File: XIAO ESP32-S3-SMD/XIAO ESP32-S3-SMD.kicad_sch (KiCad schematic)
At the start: 12 parts, among them J1 Conn_01x04_Socket, J2 Conn_01x03_Socket, J3 Conn_01x04_Socket, J4 Conn_01x03_Socket, J5 Conn_01x03_Socket, J6 Conn_01x02_Pin, U2 XIAO-ESP32-S3-SMD

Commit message: ライブラリ用ディレクトリの作成
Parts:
- J1, J3: footprint Connector_JST:JST_XH_B4B-XH-AM_1x04_P2.50mm_Vertical -> Connector_JST:JST_XH_B4B-XH-A_1x04_P2.50mm_Vertical
- J2, J4, J5: footprint Connector_JST:JST_XH_B3B-XH-AM_1x03_P2.50mm_Vertical -> Connector_JST:JST_XH_B3B-XH-A_1x03_P2.50mm_Vertical
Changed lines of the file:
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@@
 			)
 		)
-		(property "Footprint" "Connector_JST:JST_XH_B3B-XH-AM_1x03_P2.50mm_Vertical"
+		(property "Footprint" "Connector_JST:JST_XH_B3B-XH-A_1x03_P2.50mm_Vertical"
 			(at 284.48 34.29 0)
 			(hide yes)
@@
 			)
 		)
-		(property "Footprint" "Connector_JST:JST_XH_B4B-XH-AM_1x04_P2.50mm_Vertical"
+		(property "Footprint" "Connector_JST:JST_XH_B4B-XH-A_1x04_P2.50mm_Vertical"
 			(at 294.64 130.81 0)
 			(hide yes)
@@
 			)
 		)
-		(property "Footprint" "Connector_JST:JST_XH_B3B-XH-AM_1x03_P2.50mm_Vertical"
+		(property "Footprint" "Connector_JST:JST_XH_B3B-XH-A_1x03_P2.50mm_Vertical"
 			(at 284.48 66.04 0)
 			(hide yes)
@@
 			)
 		)
-		(property "Footprint" "Connector_JST:JST_XH_B4B-XH-AM_1x04_P2.50mm_Vertical"
+		(property "Footprint" "Connector_JST:JST_XH_B4B-XH-A_1x04_P2.50mm_Vertical"
 			(at 294.64 118.11 0)
 			(hide yes)
@@
 			)
 		)
-		(property "Footprint" "Connector_JST:JST_XH_B3B-XH-AM_1x03_P2.50mm_Vertical"
+		(property "Footprint" "Connector_JST:JST_XH_B3B-XH-A_1x03_P2.50mm_Vertical"
 			(at 284.48 50.8 0)
 			(hide yes)

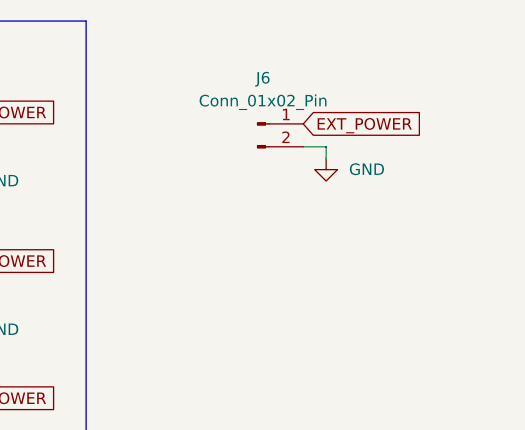
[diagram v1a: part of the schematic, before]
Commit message: 電源ライン配線前
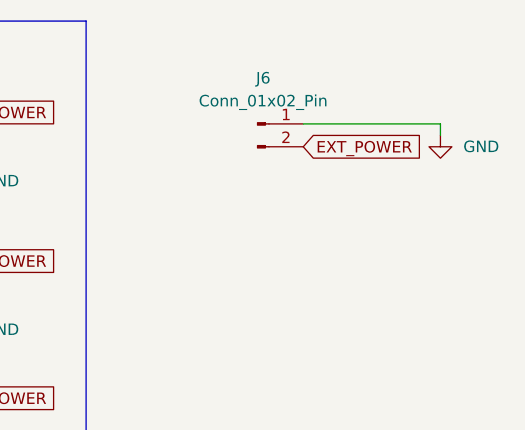
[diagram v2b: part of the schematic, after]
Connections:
- net EXT_POWER: now also J6.2 (Pin_2); no longer J6.1 (Pin_1)
- net GND: now also J6.1 (Pin_1); no longer J6.2 (Pin_2)
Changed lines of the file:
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@@
-	(wire
-		(pts
-			(xy 330.2 35.56) (xy 332.74 35.56)
-		)
-		(stroke
-			(width 0)
-			(type default)
-		)
-	)
 	(wire
 		(pts
@@
 	(wire
 		(pts
+			(xy 345.44 33.02) (xy 330.2 33.02)
+		)
+		(stroke
+			(width 0)
+			(type default)
+		)
+	)
+	(wire
+		(pts
 			(xy 203.2 107.95) (xy 196.85 107.95)
 		)
@@
 	(wire
 		(pts
-			(xy 332.74 35.56) (xy 332.74 36.83)
+			(xy 345.44 33.02) (xy 345.44 34.29)
 		)
 		(stroke
@@
 		)
 	)
+	(global_label "EXT_POWER"
+		(shape input)
+		(at 330.2 35.56 0)
+		(fields_autoplaced yes)
+		(effects
+			(font
+				(size 1.27 1.27)
+			)
+			(justify left)
+		)
+		(property "Intersheetrefs" "${INTERSHEET_REFS}"
+			(at 343.9498 35.56 0)
+			(hide yes)
+			(show_name no)
+			(do_not_autoplace no)
+			(effects
+				(font
+					(size 1.27 1.27)
+				)
+				(justify left)
+			)
+		)
+	)
 	(global_label "GPIO5"
 		(shape input)
@@
 		(property "Intersheetrefs" "${INTERSHEET_REFS}"
 			(at 223.6628 54.61 0)
-			(hide yes)
-			(show_name no)
-			(do_not_autoplace no)
-			(effects
-				(font
-					(size 1.27 1.27)
-				)
-				(justify left)
-			)
-		)
-	)
-	(global_label "EXT_POWER"
-		(shape input)
-		(at 330.2 33.02 0)
-		(fields_autoplaced yes)
-		(effects
-			(font
-				(size 1.27 1.27)
-			)
-			(justify left)
-		)
-		(property "Intersheetrefs" "${INTERSHEET_REFS}"
-			(at 343.9498 33.02 0)
 			(hide yes)
 			(show_name no)
@@
 	(symbol
 		(lib_id "power:GND")
-		(at 332.74 36.83 0)
+		(at 345.44 34.29 0)
 		(unit 1)
 		(body_style 1)
@@
 		(fields_autoplaced yes)
 		(property "Reference" "#PWR05"
-			(at 332.74 43.18 0)
+			(at 345.44 40.64 0)
 			(hide yes)
 			(show_name no)
@@
 		)
 		(property "Value" "GND"
-			(at 335.28 38.0999 0)
+			(at 347.98 35.5599 0)
 			(show_name no)
 			(do_not_autoplace no)
@@
 		)
 		(property "Footprint" ""
-			(at 332.74 36.83 0)
+			(at 345.44 34.29 0)
 			(hide yes)
 			(show_name no)
@@
 		)
 		(property "Datasheet" ""
-			(at 332.74 36.83 0)
+			(at 345.44 34.29 0)
 			(hide yes)
 			(show_name no)
@@
 		)
 		(property "Description" ""
-			(at 332.74 36.83 0)
-			(hide yes)
-			(show_name no)
+			(at 345.44 34.29 0)
+			(hide yes)
+			(show_name no)
